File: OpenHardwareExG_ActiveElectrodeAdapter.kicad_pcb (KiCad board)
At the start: 4 copper layers, 126.7 x 59.7 mm, 22 parts, among them P1 CONN_01X03, P10 CONN_01X03, P11 CONN_01X03, P12 CONN_01X03, P13 CONN_01X03, P14 CONN_01X03, P15 CONN_01X03, P16 CONN_01X03, P17 CONN_01X20, P18 CONN_01X18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

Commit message: add RLD
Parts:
- added P19: CONN_01X01, Pin_Headers:Pin_Header_Straight_1x01, F.Cu at (86.4, 49.5)
- added Touchproof-socket: VAL**, Touchproof-socket-spacer, F.Cu at (86.4, 58.4)
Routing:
- net /RLD: track 106.7 -> 118.1 mm
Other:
- board text removed: "TODO: ADD RLD hole/Connector"
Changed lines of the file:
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@@
-(kicad_pcb (version 4) (host pcbnew 4.0.1-4.201602132031+6195~38~ubuntu14.04.1-stable)
+(kicad_pcb (version 4) (host pcbnew 4.0.2-4+6225~38~ubuntu14.04.1-stable)
   (general
-    (links 67)
+    (links 68)
     (no_connects 0)
-    (area 79.054999 9.414999 234.275001 128.8)
+    (area 76.124999 27.39412 202.970201 89.79626)
     (thickness 1.6)
-    (drawings 5)
-    (tracks 199)
+    (drawings 4)
+    (tracks 200)
     (zones 0)
-    (modules 22)
+    (modules 24)
     (nets 20)
   )
@@
     (add_net /VCC)
   )
+  (module Touchproof-socket-spacer (layer F.Cu)
+    (at 86.36 58.42)
+    (fp_text reference Touchproof-socket (at 0 -6.35) (layer F.SilkS) hide
+      (effects (font (thickness 0.3048)))
+    )
+    (fp_text value VAL** (at 0 6.35) (layer F.SilkS) hide
+      (effects (font (thickness 0.3048)))
+    )
+    (fp_circle (center 0 0) (end 4.8006 0) (layer F.SilkS) (width 0.381))
+    (pad "" thru_hole circle (at 0 0) (size 7.92988 7.92988) (drill 7.92988) (layers *.Cu))
+  )
   (module active_electrode_connectors:DF50A-3P-1V (layer F.Cu)
     (at 100.24 36.82 270)
@@
     (pad 1 thru_hole circle (at 0 0) (size 3.5 3.5) (drill 3.5) (layers))
   )
-  (gr_text "TODO:\nADD RLD\nhole/Connector " (at 88.265 44.45) (layer F.SilkS)
-    (effects (font (size 1.5 1.5) (thickness 0.3)))
+  (module Pin_Headers:Pin_Header_Straight_1x01 (layer F.Cu)
+    (at 86.36 49.53)
+    (descr "Through hole pin header")
+    (tags "pin header")
+    (fp_text reference P19 (at 0 -5.1) (layer F.SilkS)
+      (effects (font (size 1 1) (thickness 0.15)))
+    )
+    (fp_text value CONN_01X01 (at 0 -3.1) (layer F.Fab)
+      (effects (font (size 1 1) (thickness 0.15)))
+    )
+    (fp_line (start 1.55 -1.55) (end 1.55 0) (layer F.SilkS) (width 0.15))
+    (fp_line (start -1.75 -1.75) (end -1.75 1.75) (layer F.CrtYd) (width 0.05))
+    (fp_line (start 1.75 -1.75) (end 1.75 1.75) (layer F.CrtYd) (width 0.05))
+    (fp_line (start -1.75 -1.75) (end 1.75 -1.75) (layer F.CrtYd) (width 0.05))
+    (fp_line (start -1.75 1.75) (end 1.75 1.75) (layer F.CrtYd) (width 0.05))
+    (fp_line (start -1.55 0) (end -1.55 -1.55) (layer F.SilkS) (width 0.15))
+    (fp_line (start -1.55 -1.55) (end 1.55 -1.55) (layer F.SilkS) (width 0.15))
+    (fp_line (start -1.27 1.27) (end 1.27 1.27) (layer F.SilkS) (width 0.15))
+    (pad 1 thru_hole rect (at 0 0) (size 2.2352 2.2352) (drill 1.016) (layers *.Cu *.Mask F.SilkS)
+      (net 19 /RLD))
+    (model Pin_Headers.3dshapes/Pin_Header_Straight_1x01.wrl
+      (at (xyz 0 0 0))
+      (scale (xyz 1 1 1))
+      (rotate (xyz 0 0 90))
+    )
   )
   (gr_line (start 76.2 88.9) (end 202.8952 88.9) (angle 90) (layer Edge.Cuts) (width 0.15))
@@
   (via (at 168.275 55.88) (size 0.6) (drill 0.4) (layers F.Cu B.Cu) (net 18))
   (segment (start 193.04 55.88) (end 177.8 55.88) (width 0.25) (layer B.Cu) (net 18))
-  (segment (start 177.8 38.1) (end 86.36 38.1) (width 0.25) (layer B.Cu) (net 19))
+  (segment (start 86.36 49.53) (end 86.36 38.1) (width 0.25) (layer F.Cu) (net 19))
   (via (at 86.36 38.1) (size 0.6) (drill 0.4) (layers F.Cu B.Cu) (net 19))
+  (segment (start 86.36 38.1) (end 177.8 38.1) (width 0.25) (layer B.Cu) (net 19))
   (segment (start 193.04 38.1) (end 177.8 38.1) (width 0.25) (layer B.Cu) (net 19))
   (zone (net 1) (net_name /VCC) (layer In1.Cu) (hatch edge 0.508)

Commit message: add labels for electrodes
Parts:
- moved P19 5.08 mm to (86.4, 44.5), turned to 180 degrees
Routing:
- net /RLD: track 118.1 -> 113.0 mm
- net /IN6P: track 65.1 -> 64.6 mm, vias 3 -> 1
- net /VCC: track 43.4 -> 43.9 mm
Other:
- board text added: "BIAS OUT"
- board text added: "IN 1+"
- board text added: "IN 1-"
- board text added: "IN 2+"
- board text added: "IN 2-"
- board text added: "IN 3+"
- board text added: "IN 3-"
- board text added: "IN 4+"
- board text added: "IN 4-"
- board text added: "IN 5+"
- board text added: "IN 5-"
- board text added: "IN 6+"
- board text added: "IN 6-"
- board text added: "IN 7+"
- board text added: "IN 7-"
- board text added: "IN 8+"
- board text added: "IN 8-"
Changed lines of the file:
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@@
     (links 68)
     (no_connects 0)
-    (area 76.124999 27.39412 202.970201 89.79626)
+    (area 75.121886 27.39412 202.970201 89.79626)
     (thickness 1.6)
-    (drawings 4)
-    (tracks 200)
+    (drawings 21)
+    (tracks 201)
     (zones 0)
     (modules 24)
@@
     (mod_text_size 1 1)
     (mod_text_width 0.15)
-    (pad_size 1.524 1.524)
-    (pad_drill 0.762)
+    (pad_size 7.92988 7.92988)
+    (pad_drill 7.92988)
     (pad_to_mask_clearance 0.2)
     (aux_axis_origin 0 0)
@@
       (effects (font (thickness 0.3048)))
     )
-    (fp_text value VAL** (at 0 6.35) (layer F.SilkS) hide
+    (fp_text value VAL** (at -6.36 9.58) (layer F.SilkS) hide
       (effects (font (thickness 0.3048)))
     )
@@
   (module active_electrode_connectors:DF50A-3P-1V (layer F.Cu)
     (at 100.24 51.82 270)
-    (fp_text reference P2 (at -1.5 -1.5 360) (layer F.SilkS)
+    (fp_text reference P2 (at -1.5 -1.5 450) (layer F.SilkS)
       (effects (font (size 1 1) (thickness 0.15)))
     )
@@
   (module active_electrode_connectors:DF50A-3P-1V (layer F.Cu)
     (at 140.24 66.82 270)
-    (fp_text reference P11 (at -1.5 -1.5 360) (layer F.SilkS)
+    (fp_text reference P11 (at -1.5 -1.5 450) (layer F.SilkS)
       (effects (font (size 1 1) (thickness 0.15)))
     )
@@
   (module active_electrode_connectors:DF50A-3P-1V (layer F.Cu)
     (at 160.24 66.82 270)
-    (fp_text reference P15 (at -1.5 -1.5 360) (layer F.SilkS)
+    (fp_text reference P15 (at -1.5 -1.5 450) (layer F.SilkS)
       (effects (font (size 1 1) (thickness 0.15)))
     )
@@
   )
   (module Pin_Headers:Pin_Header_Straight_1x01 (layer F.Cu)
-    (at 86.36 49.53)
+    (at 86.36 44.45 180)
     (descr "Through hole pin header")
     (tags "pin header")
-    (fp_text reference P19 (at 0 -5.1) (layer F.SilkS)
-      (effects (font (size 1 1) (thickness 0.15)))
-    )
-    (fp_text value CONN_01X01 (at 0 -3.1) (layer F.Fab)
+    (fp_text reference P19 (at 0 -5.1 180) (layer F.SilkS)
+      (effects (font (size 1 1) (thickness 0.15)))
+    )
+    (fp_text value CONN_01X01 (at 0 -3.1 180) (layer F.Fab)
       (effects (font (size 1 1) (thickness 0.15)))
     )
@@
     (fp_line (start -1.55 -1.55) (end 1.55 -1.55) (layer F.SilkS) (width 0.15))
     (fp_line (start -1.27 1.27) (end 1.27 1.27) (layer F.SilkS) (width 0.15))
-    (pad 1 thru_hole rect (at 0 0) (size 2.2352 2.2352) (drill 1.016) (layers *.Cu *.Mask F.SilkS)
+    (pad 1 thru_hole rect (at 0 0 180) (size 2.2352 2.2352) (drill 1.016) (layers *.Cu *.Mask F.SilkS)
       (net 19 /RLD))
     (model Pin_Headers.3dshapes/Pin_Header_Straight_1x01.wrl
@@
     )
   )
+  (gr_text "BIAS\nOUT" (at 86.36 67) (layer F.SilkS)
+    (effects (font (size 1.5 1.5) (thickness 0.3)))
+  )
+  (gr_text "IN 6+" (at 144 67 90) (layer F.SilkS)
+    (effects (font (size 1.5 1.5) (thickness 0.3)))
+  )
+  (gr_text "IN 5+" (at 144 82 90) (layer F.SilkS)
+    (effects (font (size 1.5 1.5) (thickness 0.3)))
+  )
+  (gr_text "IN 7+" (at 144 52 90) (layer F.SilkS)
+    (effects (font (size 1.5 1.5) (thickness 0.3)))
+  )
+  (gr_text "IN 8+" (at 144 37 90) (layer F.SilkS)
+    (effects (font (size 1.5 1.5) (thickness 0.3)))
+  )
+  (gr_text "IN 8-" (at 164 37 90) (layer F.SilkS)
+    (effects (font (size 1.5 1.5) (thickness 0.3)))
+  )
+  (gr_text "IN 7-" (at 164 52 90) (layer F.SilkS)
+    (effects (font (size 1.5 1.5) (thickness 0.3)))
+  )
+  (gr_text "IN 5-" (at 164 82 90) (layer F.SilkS)
+    (effects (font (size 1.5 1.5) (thickness 0.3)))
+  )
+  (gr_text "IN 6-" (at 164 67 90) (layer F.SilkS)
+    (effects (font (size 1.5 1.5) (thickness 0.3)))
+  )
+  (gr_text "IN 2-" (at 124 67 90) (layer F.SilkS)
+    (effects (font (size 1.5 1.5) (thickness 0.3)))
+  )
+  (gr_text "IN 1-" (at 124 82 90) (layer F.SilkS)
+    (effects (font (size 1.5 1.5) (thickness 0.3)))
+  )
+  (gr_text "IN 3-" (at 124 52 90) (layer F.SilkS)
+    (effects (font (size 1.5 1.5) (thickness 0.3)))
+  )
+  (gr_text "IN 4-" (at 124 37 90) (layer F.SilkS)
+    (effects (font (size 1.5 1.5) (thickness 0.3)))
+  )
+  (gr_text "IN 4+" (at 104 37 90) (layer F.SilkS)
+    (effects (font (size 1.5 1.5) (thickness 0.3)))
+  )
+  (gr_text "IN 3+" (at 104 52 90) (layer F.SilkS)
+    (effects (font (size 1.5 1.5) (thickness 0.3)))
+  )
+  (gr_text "IN 1+" (at 104 82 90) (layer F.SilkS)
+    (effects (font (size 1.5 1.5) (thickness 0.3)))
+  )
+  (gr_text "IN 2+" (at 104 67 90) (layer F.SilkS)
+    (effects (font (size 1.5 1.5) (thickness 0.3)))
+  )
   (gr_line (start 76.2 88.9) (end 202.8952 88.9) (angle 90) (layer Edge.Cuts) (width 0.15))
   (gr_line (start 76.2 29.21) (end 202.8952 29.21) (angle 90) (layer Edge.Cuts) (width 0.15))
   (gr_line (start 76.2 29.21) (end 76.2 88.9) (angle 90) (layer Edge.Cuts) (width 0.15))
   (gr_line (start 202.8952 29.21) (end 202.8952 88.9) (angle 90) (layer Edge.Cuts) (width 0.15))
+  (via (at 157.806941 52.219982) (size 0.6) (drill 0.4) (layers F.Cu B.Cu) (net 1))
+  (segment (start 158.614982 52.219982) (end 158.231205 52.219982) (width 0.25) (layer F.Cu) (net 1))
+  (segment (start 159.215 52.82) (end 158.614982 52.219982) (width 0.25) (layer F.Cu) (net 1))
+  (segment (start 160.24 52.82) (end 159.215 52.82) (width 0.25) (layer F.Cu) (net 1))
+  (segment (start 158.231205 52.219982) (end 157.806941 52.219982) (width 0.25) (layer F.Cu) (net 1))
   (segment (start 140.24 67.82) (end 138.305 67.82) (width 0.25) (layer F.Cu) (net 1))
   (via (at 137.795 67.31) (size 0.6) (drill 0.4) (layers F.Cu B.Cu) (net 1))
@@
   (via (at 157.48 67.31) (size 0.6) (drill 0.4) (layers F.Cu B.Cu) (net 1))
   (segment (start 157.99 67.82) (end 157.48 67.31) (width 0.25) (layer F.Cu) (net 1))
-  (segment (start 160.24 52.82) (end 158.23 52.82) (width 0.25) (layer F.Cu) (net 1))
-  (via (at 158.115 52.705) (size 0.6) (drill 0.4) (layers F.Cu B.Cu) (net 1))
-  (segment (start 158.23 52.82) (end 158.115 52.705) (width 0.25) (layer F.Cu) (net 1))
   (segment (start 160.24 37.82) (end 158.47 37.82) (width 0.25) (layer F.Cu) (net 1))
   (via (at 157.48 36.83) (size 0.6) (drill 0.4) (layers F.Cu B.Cu) (net 1))
@@
   (via (at 143.51 48.26) (size 0.6) (drill 0.4) (layers F.Cu B.Cu) (net 12))
   (segment (start 193.04 48.26) (end 177.8 48.26) (width 0.25) (layer B.Cu) (net 12))
-  (segment (start 177.8 53.34) (end 163.83 53.34) (width 0.25) (layer B.Cu) (net 13))
-  (segment (start 142.095 66.82) (end 140.24 66.82) (width 0.25) (layer F.Cu) (net 13))
-  (segment (start 144.145 64.77) (end 142.095 66.82) (width 0.25) (layer F.Cu) (net 13))
-  (via (at 144.145 64.77) (size 0.6) (drill 0.4) (layers F.Cu B.Cu) (net 13))
-  (segment (start 163.83 64.77) (end 144.145 64.77) (width 0.25) (layer B.Cu) (net 13))
-  (via (at 163.83 64.77) (size 0.6) (drill 0.4) (layers F.Cu B.Cu) (net 13))
-  (segment (start 163.83 53.34) (end 163.83 64.77) (width 0.25) (layer F.Cu) (net 13))
-  (via (at 163.83 53.34) (size 0.6) (drill 0.4) (layers F.Cu B.Cu) (net 13))
+  (segment (start 140.24 66.82) (end 142.97 66.82) (width 0.25) (layer F.Cu) (net 13))
+  (via (at 145.9 53.36) (size 0.6) (drill 0.4) (layers F.Cu B.Cu) (net 13))
+  (segment (start 145.92 53.34) (end 177.8 53.34) (width 0.25) (layer B.Cu) (net 13))
+  (segment (start 145.92 53.34) (end 145.9 53.36) (width 0.25) (layer B.Cu) (net 13))
+  (segment (start 144.42 54.84) (end 145.9 53.36) (width 0.25) (layer F.Cu) (net 13))
+  (segment (start 144.42 65.37) (end 144.42 54.84) (width 0.25) (layer F.Cu) (net 13))
+  (segment (start 142.97 66.82) (end 144.42 65.37) (width 0.25) (layer F.Cu) (net 13))
   (segment (start 193.04 53.34) (end 177.8 53.34) (width 0.25) (layer B.Cu) (net 13))
   (segment (start 177.8 58.42) (end 146.05 58.42) (width 0.25) (layer B.Cu) (net 14))
@@
   (via (at 168.275 55.88) (size 0.6) (drill 0.4) (layers F.Cu B.Cu) (net 18))
   (segment (start 193.04 55.88) (end 177.8 55.88) (width 0.25) (layer B.Cu) (net 18))
-  (segment (start 86.36 49.53) (end 86.36 38.1) (width 0.25) (layer F.Cu) (net 19))
+  (segment (start 86.36 44.45) (end 86.36 38.1) (width 0.25) (layer F.Cu) (net 19) (status 10))
   (via (at 86.36 38.1) (size 0.6) (drill 0.4) (layers F.Cu B.Cu) (net 19))
   (segment (start 86.36 38.1) (end 177.8 38.1) (width 0.25) (layer B.Cu) (net 19))

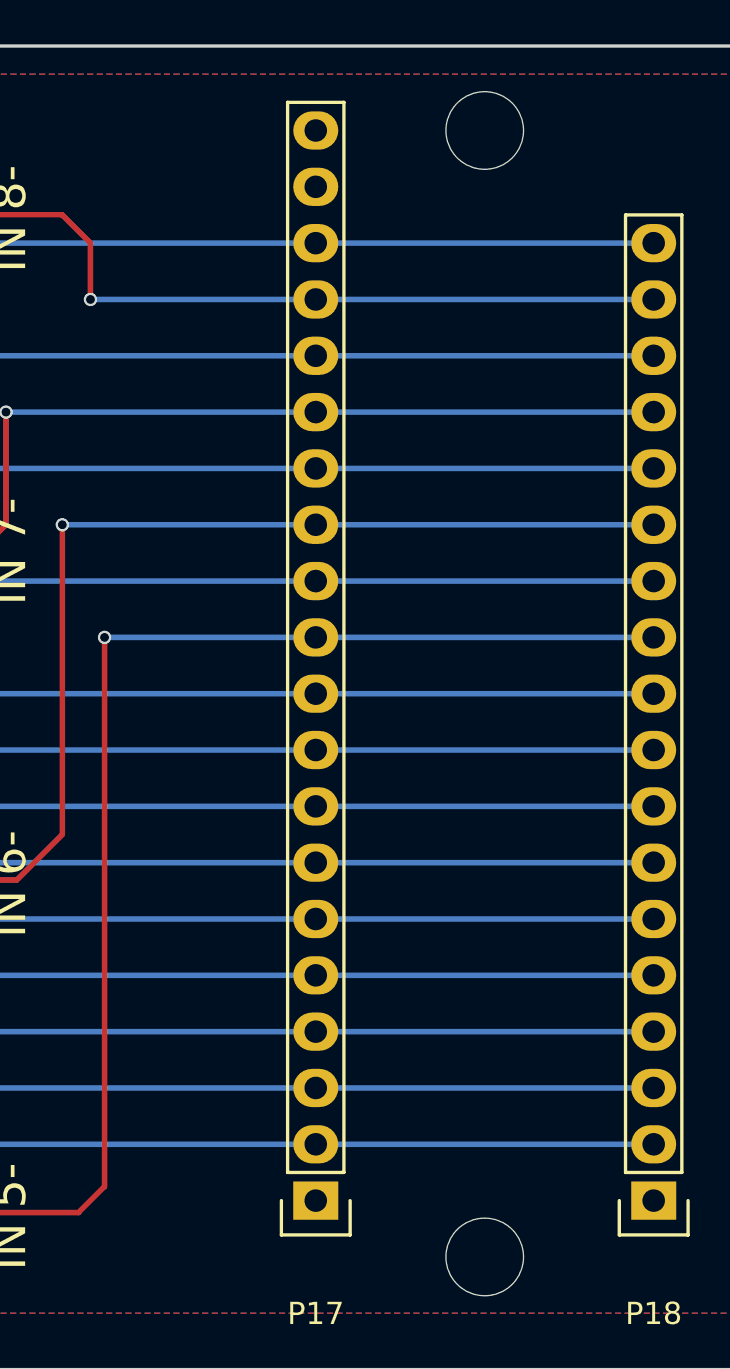
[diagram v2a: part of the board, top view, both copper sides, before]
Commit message: add labels to pins and headers
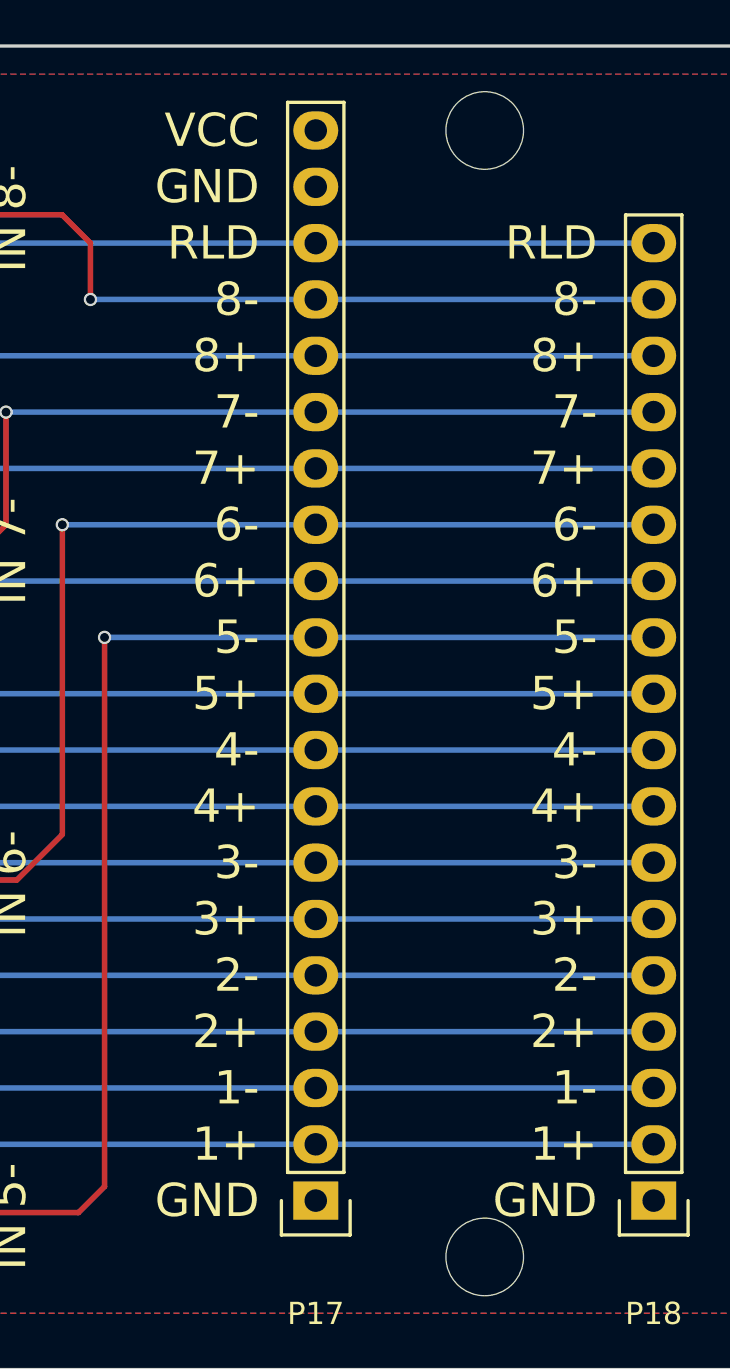
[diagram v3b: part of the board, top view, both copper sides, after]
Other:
- board text added: "1+"
- board text added: "1-"
- board text added: "2+"
- board text added: "2-"
- board text added: "3+"
- board text added: "3-"
- board text added: "4+"
- board text added: "4-"
- board text added: "5+"
- board text added: "5-"
- board text added: "6+"
- board text added: "6-"
- board text added: "7+"
- board text added: "7-"
- board text added: "8+"
- board text added: "8-"
- board text added: "GND"
- board text added: "RLD"
- board text added: "VCC"
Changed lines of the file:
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@@
     (area 75.121886 27.39412 202.970201 89.79626)
     (thickness 1.6)
-    (drawings 21)
+    (drawings 59)
     (tracks 201)
     (zones 0)
@@
     )
   )
+  (gr_text RLD (at 190.5 38.1) (layer F.SilkS)
+    (effects (font (size 1.5 1.5) (thickness 0.3)) (justify right))
+  )
+  (gr_text 8- (at 190.5 40.64) (layer F.SilkS)
+    (effects (font (size 1.5 1.5) (thickness 0.3)) (justify right))
+  )
+  (gr_text 8+ (at 190.5 43.18) (layer F.SilkS)
+    (effects (font (size 1.5 1.5) (thickness 0.3)) (justify right))
+  )
+  (gr_text 7- (at 190.5 45.72) (layer F.SilkS)
+    (effects (font (size 1.5 1.5) (thickness 0.3)) (justify right))
+  )
+  (gr_text 7+ (at 190.5 48.26) (layer F.SilkS)
+    (effects (font (size 1.5 1.5) (thickness 0.3)) (justify right))
+  )
+  (gr_text 6- (at 190.5 50.8) (layer F.SilkS)
+    (effects (font (size 1.5 1.5) (thickness 0.3)) (justify right))
+  )
+  (gr_text 6+ (at 190.5 53.34) (layer F.SilkS)
+    (effects (font (size 1.5 1.5) (thickness 0.3)) (justify right))
+  )
+  (gr_text 5- (at 190.5 55.88) (layer F.SilkS)
+    (effects (font (size 1.5 1.5) (thickness 0.3)) (justify right))
+  )
+  (gr_text 5+ (at 190.5 58.42) (layer F.SilkS)
+    (effects (font (size 1.5 1.5) (thickness 0.3)) (justify right))
+  )
+  (gr_text 4- (at 190.5 60.96) (layer F.SilkS)
+    (effects (font (size 1.5 1.5) (thickness 0.3)) (justify right))
+  )
+  (gr_text 4+ (at 190.5 63.5) (layer F.SilkS)
+    (effects (font (size 1.5 1.5) (thickness 0.3)) (justify right))
+  )
+  (gr_text 3- (at 190.5 66.04) (layer F.SilkS)
+    (effects (font (size 1.5 1.5) (thickness 0.3)) (justify right))
+  )
+  (gr_text 3+ (at 190.5 68.58) (layer F.SilkS)
+    (effects (font (size 1.5 1.5) (thickness 0.3)) (justify right))
+  )
+  (gr_text 2- (at 190.5 71.12) (layer F.SilkS)
+    (effects (font (size 1.5 1.5) (thickness 0.3)) (justify right))
+  )
+  (gr_text 2+ (at 190.5 73.66) (layer F.SilkS)
+    (effects (font (size 1.5 1.5) (thickness 0.3)) (justify right))
+  )
+  (gr_text 1- (at 190.5 76.2) (layer F.SilkS)
+    (effects (font (size 1.5 1.5) (thickness 0.3)) (justify right))
+  )
+  (gr_text 1+ (at 190.5 78.74) (layer F.SilkS)
+    (effects (font (size 1.5 1.5) (thickness 0.3)) (justify right))
+  )
+  (gr_text GND (at 190.5 81.28) (layer F.SilkS)
+    (effects (font (size 1.5 1.5) (thickness 0.3)) (justify right))
+  )
+  (gr_text GND (at 175.26 81.28) (layer F.SilkS)
+    (effects (font (size 1.5 1.5) (thickness 0.3)) (justify right))
+  )
+  (gr_text 1+ (at 175.26 78.74) (layer F.SilkS)
+    (effects (font (size 1.5 1.5) (thickness 0.3)) (justify right))
+  )
+  (gr_text 1- (at 175.26 76.2) (layer F.SilkS)
+    (effects (font (size 1.5 1.5) (thickness 0.3)) (justify right))
+  )
+  (gr_text 2+ (at 175.26 73.66) (layer F.SilkS)
+    (effects (font (size 1.5 1.5) (thickness 0.3)) (justify right))
+  )
+  (gr_text 2- (at 175.26 71.12) (layer F.SilkS)
+    (effects (font (size 1.5 1.5) (thickness 0.3)) (justify right))
+  )
+  (gr_text 3+ (at 175.26 68.58) (layer F.SilkS)
+    (effects (font (size 1.5 1.5) (thickness 0.3)) (justify right))
+  )
+  (gr_text 3- (at 175.26 66.04) (layer F.SilkS)
+    (effects (font (size 1.5 1.5) (thickness 0.3)) (justify right))
+  )
+  (gr_text 4+ (at 175.26 63.5) (layer F.SilkS)
+    (effects (font (size 1.5 1.5) (thickness 0.3)) (justify right))
+  )
+  (gr_text 4- (at 175.26 60.96) (layer F.SilkS)
+    (effects (font (size 1.5 1.5) (thickness 0.3)) (justify right))
+  )
+  (gr_text 5+ (at 175.26 58.42) (layer F.SilkS)
+    (effects (font (size 1.5 1.5) (thickness 0.3)) (justify right))
+  )
+  (gr_text 5- (at 175.26 55.88) (layer F.SilkS)
+    (effects (font (size 1.5 1.5) (thickness 0.3)) (justify right))
+  )
+  (gr_text 6+ (at 175.26 53.34) (layer F.SilkS)
+    (effects (font (size 1.5 1.5) (thickness 0.3)) (justify right))
+  )
+  (gr_text 6- (at 175.26 50.8) (layer F.SilkS)
+    (effects (font (size 1.5 1.5) (thickness 0.3)) (justify right))
+  )
+  (gr_text 7+ (at 175.26 48.26) (layer F.SilkS)
+    (effects (font (size 1.5 1.5) (thickness 0.3)) (justify right))
+  )
+  (gr_text 7- (at 175.26 45.72) (layer F.SilkS)
+    (effects (font (size 1.5 1.5) (thickness 0.3)) (justify right))
+  )
+  (gr_text 8+ (at 175.26 43.18) (layer F.SilkS)
+    (effects (font (size 1.5 1.5) (thickness 0.3)) (justify right))
+  )
+  (gr_text 8- (at 175.26 40.64) (layer F.SilkS)
+    (effects (font (size 1.5 1.5) (thickness 0.3)) (justify right))
+  )
+  (gr_text RLD (at 175.26 38.1) (layer F.SilkS)
+    (effects (font (size 1.5 1.5) (thickness 0.3)) (justify right))
+  )
+  (gr_text GND (at 175.26 35.56) (layer F.SilkS)
+    (effects (font (size 1.5 1.5) (thickness 0.3)) (justify right))
+  )
+  (gr_text VCC (at 175.26 33.02) (layer F.SilkS)
+    (effects (font (size 1.5 1.5) (thickness 0.3)) (justify right))
+  )
   (gr_text "BIAS\nOUT" (at 86.36 67) (layer F.SilkS)
